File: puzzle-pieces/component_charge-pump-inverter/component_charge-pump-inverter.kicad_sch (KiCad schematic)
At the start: 11 parts, among them J1 Conn_01x02_Pin, J2 Conn_01x02_Pin, J3 Conn_01x02_Pin

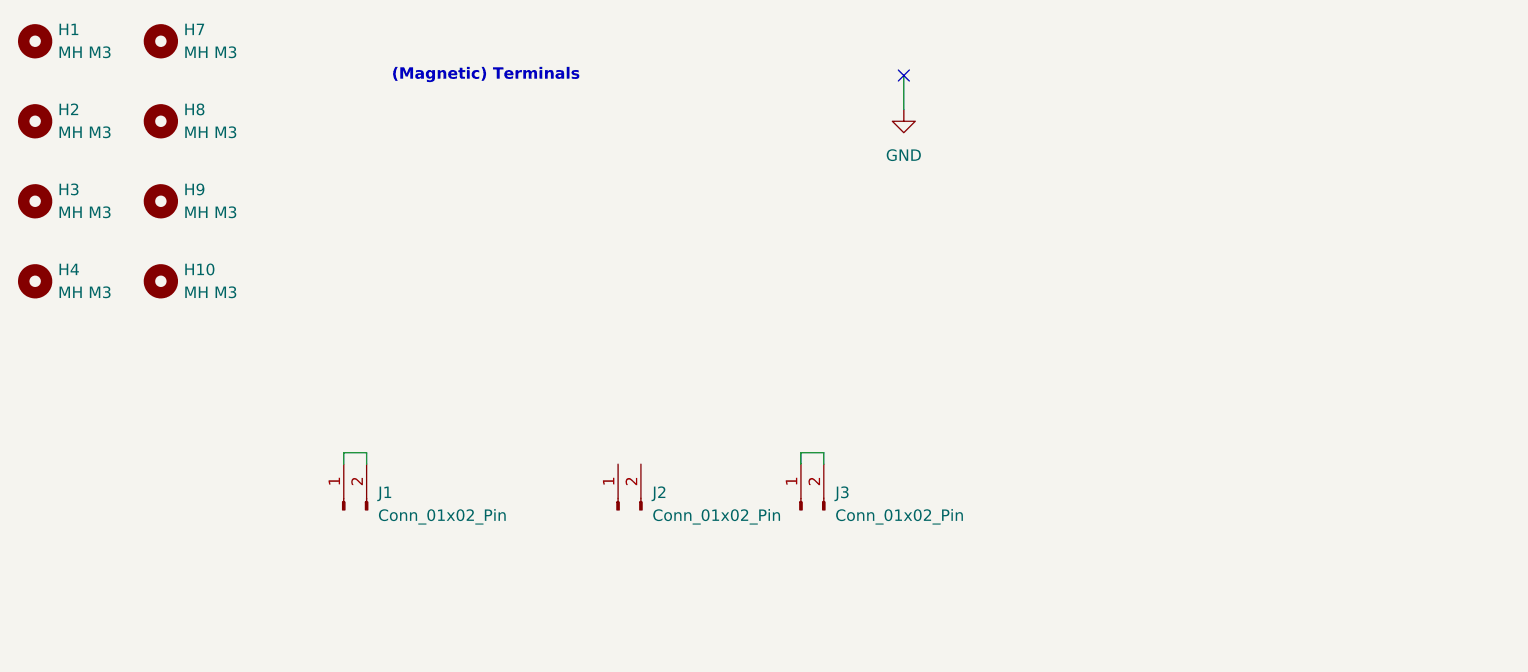
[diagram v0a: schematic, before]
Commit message: Update PCB storage and inverter component files
Modified STEP and FreeCAD files for PCB storage system, updated .gitignore to include new backup patterns, and replaced charge-pump inverter KiCad files with new versions and documentation. Added PNG renders and a ZIP archive for the inverter component, reflecting a redesign or migration of project files.
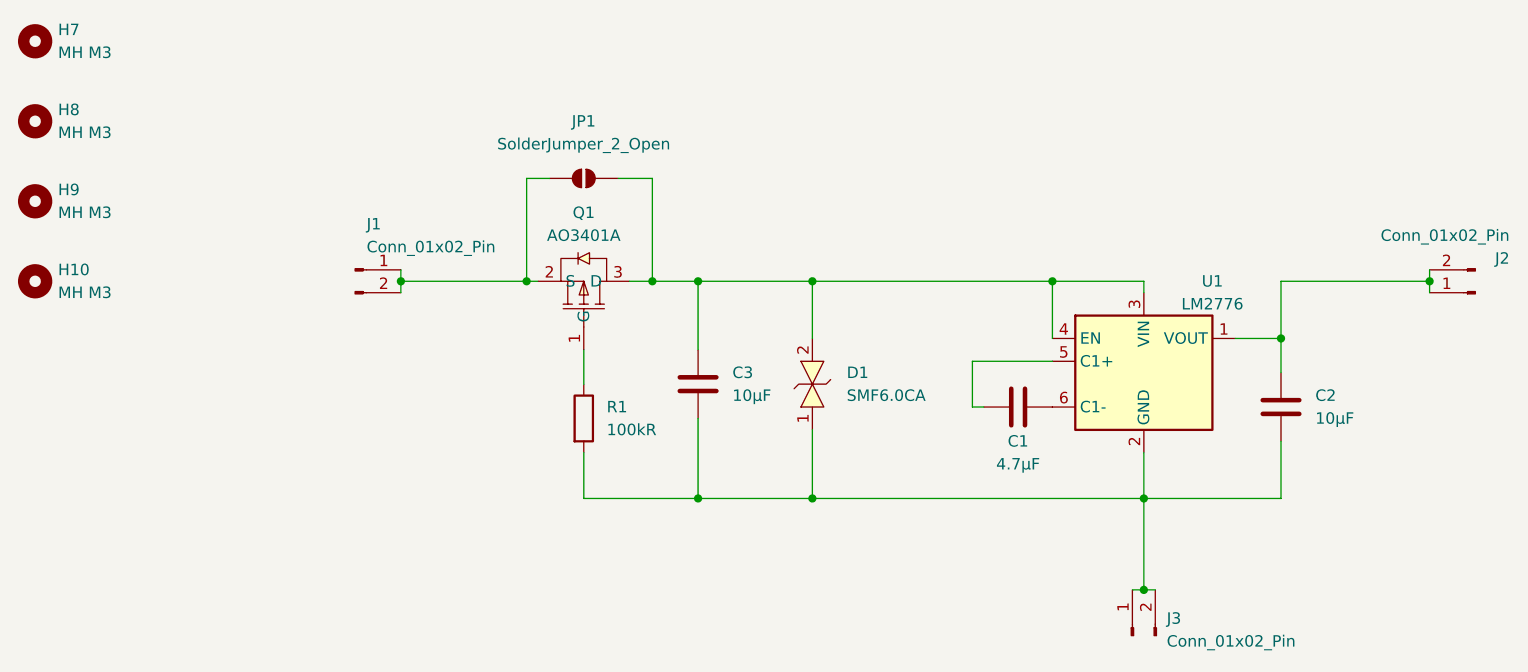
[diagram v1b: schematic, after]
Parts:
- removed H1, H2, H3, H4: MH M3, EASYEDA2KICAD:MountingHole_3.0mm_M3_tight, symbol Mechanical:MountingHole
- added C1: 4.7µF, Capacitor_SMD:C_0805_2012Metric_Pad1.18x1.45mm_HandSolder, symbol Device:C
- added C2, C3: 10µF, Capacitor_SMD:C_0805_2012Metric_Pad1.18x1.45mm_HandSolder, symbol Device:C
- added D1: SMF6.0CA, EASYEDA2KICAD:SOD-123FL_L2.8-W1.8-LS3.7-BI, symbol EASYEDA2KICAD:SMF6.0CA_C2836402
- added JP1: SolderJumper_2_Open, Jumper:SolderJumper-2_P1.3mm_Open_RoundedPad1.0x1.5mm, symbol Jumper:SolderJumper_2_Open
- added Q1: AO3401A, EASYEDA2KICAD:SOT-23-3_L2.9-W1.6-P1.90-LS2.8-BR, symbol EASYEDA2KICAD:AO3401A_C5224202
- added R1: 100kR, Resistor_SMD:R_0805_2012Metric_Pad1.20x1.40mm_HandSolder, symbol Device:R
- added U1: LM2776, Package_TO_SOT_SMD:SOT-23-6, symbol Regulator_SwitchedCapacitor:LM2776
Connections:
- net at J3.1 (Pin_1), J3.2 (Pin_2): now also C2.2, C3.2, D1.1, R1.2, U1.2 (GND)
- net at J1.1 (Pin_1), J1.2 (Pin_2): now also JP1.1 (A), Q1.2 (S)
- net at J2.1 (Pin_1): now also J2.2 (Pin_2), C2.1, U1.1 (VOUT)
- new net: C3.1, D1.2, JP1.2 (B), Q1.3 (D), U1.3 (VIN), U1.4 (EN)
- new net: C1.1, U1.5 (C1+)
- new net: C1.2, U1.6 (C1-)
- new net: Q1.1 (G), R1.1
- no-connect marks 1 -> 0
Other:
- note removed: "(Magnetic) Terminals"
- moved on the sheet: H10, H7, H8, H9, J1, J2, J3

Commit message: Update charge-pump inverter PCB and schematic
Adjusted several PCB graphic line coordinates for improved layout accuracy. Added LCSC part number property to schematic. Included updated production ZIP for manufacturing.
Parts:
- R1: LCSC (none) -> C149504
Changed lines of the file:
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@@
+			)
+		)
+		(property "LCSC" "C149504"
+			(at 76.2 57.15 0)
+			(effects
+				(font
+					(size 1.27 1.27)
+				)
+				(hide yes)
 			)
 		)
